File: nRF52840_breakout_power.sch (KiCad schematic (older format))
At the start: 18 parts, among them J7 Conn_01x02, Q1 DMG2395, SW1 SW_Push, U3 AP2112K-3.3, U4 MCP73831-2-OT

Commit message: changed crystal load capacitance according to component / minor changes
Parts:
- C29, C30, C31, C32: footprint (none) -> Capacitor_SMD:C_0805_2012Metric_Pad1.15x1.40mm_HandSolder
- D2: footprint (none) -> Diode_SMD:D_SOD-123F
- D3: footprint (none) -> LED_SMD:LED_0805_2012Metric_Pad1.15x1.40mm_HandSolder
- J7: value Conn_01x02 -> JST PH; footprint (none) -> Connector_JST:JST_PH_B2B-PH-SM4-TB_1x02-1MP_P2.00mm_Vertical
- Q1: footprint (none) -> Package_TO_SOT_SMD:SOT-23
- R10, R11, R5, R6, R7, R8, R9: footprint (none) -> Resistor_SMD:R_0805_2012Metric_Pad1.15x1.40mm_HandSolder
- SW1: footprint (none) -> Button_Switch_SMD:SW_SPST_EVQP7A
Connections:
- wire segments 56 -> 54
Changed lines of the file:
@@
 L Connector_Generic:Conn_01x02 J7
 U 1 1 5C935480
-P 1300 1700
-F 0 "J7" H 1220 1375 50  0000 C CNN
-F 1 "Conn_01x02" H 1220 1466 50  0000 C CNN
-F 2 "" H 1300 1700 50  0001 C CNN
-F 3 "~" H 1300 1700 50  0001 C CNN
-	1    1300 1700
+P 1350 1700
+F 0 "J7" H 1270 1375 50  0000 C CNN
+F 1 "JST PH" H 1270 1466 50  0000 C CNN
+F 2 "Connector_JST:JST_PH_B2B-PH-SM4-TB_1x02-1MP_P2.00mm_Vertical" H 1350 1700 50  0001 C CNN
+F 3 "~" H 1350 1700 50  0001 C CNN
+	1    1350 1700
 	-1   0    0    1
 $EndComp
@@
 F 0 "Q1" H 5555 1596 50  0000 L CNN
 F 1 "DMG2395" H 5555 1505 50  0000 L CNN
-F 2 "" H 5550 1475 50  0001 L CIN
+F 2 "Package_TO_SOT_SMD:SOT-23" H 5550 1475 50  0001 L CIN
 F 3 "http://www.vishay.com/docs/70209/70209.pdf" H 5350 1550 50  0001 L CNN
 	1    5350 1550
@@
 F 0 "D2" H 5200 1784 50  0000 C CNN
 F 1 "MBR120" H 5200 1875 50  0000 C CNN
-F 2 "" H 5200 2000 50  0001 C CNN
+F 2 "Diode_SMD:D_SOD-123F" H 5200 2000 50  0001 C CNN
 F 3 "~" H 5200 2000 50  0001 C CNN
 	1    5200 2000
@@
 F 0 "R8" H 4742 2304 50  0000 R CNN
 F 1 "100k" H 4742 2395 50  0000 R CNN
-F 2 "" H 4800 2350 50  0001 C CNN
+F 2 "Resistor_SMD:R_0805_2012Metric_Pad1.15x1.40mm_HandSolder" H 4800 2350 50  0001 C CNN
 F 3 "~" H 4800 2350 50  0001 C CNN
 	1    4800 2350
@@
 F 0 "C30" H 5542 2396 50  0000 L CNN
 F 1 "10µF" H 5542 2305 50  0000 L CNN
-F 2 "" H 5450 2350 50  0001 C CNN
+F 2 "Capacitor_SMD:C_0805_2012Metric_Pad1.15x1.40mm_HandSolder" H 5450 2350 50  0001 C CNN
 F 3 "~" H 5450 2350 50  0001 C CNN
 	1    5450 2350
@@
 F 0 "R9" H 5992 2304 50  0000 R CNN
 F 1 "100k" H 5992 2395 50  0000 R CNN
-F 2 "" H 6050 2350 50  0001 C CNN
+F 2 "Resistor_SMD:R_0805_2012Metric_Pad1.15x1.40mm_HandSolder" H 6050 2350 50  0001 C CNN
 F 3 "~" H 6050 2350 50  0001 C CNN
 	1    6050 2350
@@
 F 0 "C31" H 7242 2196 50  0000 L CNN
 F 1 "10µF" H 7242 2105 50  0000 L CNN
-F 2 "" H 7150 2150 50  0001 C CNN
+F 2 "Capacitor_SMD:C_0805_2012Metric_Pad1.15x1.40mm_HandSolder" H 7150 2150 50  0001 C CNN
 F 3 "~" H 7150 2150 50  0001 C CNN
 	1    7150 2150
@@
 F 0 "R11" H 10459 1496 50  0000 L CNN
 F 1 "5k" H 10459 1405 50  0000 L CNN
-F 2 "" H 10400 1450 50  0001 C CNN
+F 2 "Resistor_SMD:R_0805_2012Metric_Pad1.15x1.40mm_HandSolder" H 10400 1450 50  0001 C CNN
 F 3 "~" H 10400 1450 50  0001 C CNN
 	1    10400 1450
@@
 F 0 "C32" H 9392 1996 50  0000 L CNN
 F 1 "10µF" H 9392 1905 50  0000 L CNN
-F 2 "" H 9300 1950 50  0001 C CNN
+F 2 "Capacitor_SMD:C_0805_2012Metric_Pad1.15x1.40mm_HandSolder" H 9300 1950 50  0001 C CNN
 F 3 "~" H 9300 1950 50  0001 C CNN
 	1    9300 1950
@@
 F 0 "D3" H 8792 1295 50  0000 C CNN
 F 1 "LED" H 8792 1386 50  0000 C CNN
-F 2 "" H 8800 1550 50  0001 C CNN
+F 2 "LED_SMD:LED_0805_2012Metric_Pad1.15x1.40mm_HandSolder" H 8800 1550 50  0001 C CNN
 F 3 "~" H 8800 1550 50  0001 C CNN
 	1    8800 1550
@@
 F 0 "R10" V 9004 1550 50  0000 C CNN
 F 1 "100k" V 9095 1550 50  0000 C CNN
-F 2 "" H 9200 1550 50  0001 C CNN
+F 2 "Resistor_SMD:R_0805_2012Metric_Pad1.15x1.40mm_HandSolder" H 9200 1550 50  0001 C CNN
 F 3 "~" H 9200 1550 50  0001 C CNN
 	1    9200 1550
@@
 F 0 "R7" H 3242 1804 50  0000 R CNN
 F 1 "100k" H 3242 1895 50  0000 R CNN
-F 2 "" H 3300 1850 50  0001 C CNN
+F 2 "Resistor_SMD:R_0805_2012Metric_Pad1.15x1.40mm_HandSolder" H 3300 1850 50  0001 C CNN
 F 3 "~" H 3300 1850 50  0001 C CNN
 	1    3300 1850
@@
 F 0 "R6" H 3242 1404 50  0000 R CNN
 F 1 "100k" H 3242 1495 50  0000 R CNN
-F 2 "" H 3300 1450 50  0001 C CNN
+F 2 "Resistor_SMD:R_0805_2012Metric_Pad1.15x1.40mm_HandSolder" H 3300 1450 50  0001 C CNN
 F 3 "~" H 3300 1450 50  0001 C CNN
 	1    3300 1450
@@
 Wire Wire Line
 	3300 1950 3300 2000
-Wire Wire Line
-	1500 1600 1550 1600
-Wire Wire Line
-	1500 1700 1550 1700
 Wire Wire Line
 	1550 1700 1550 1750
@@
 F 0 "SW1" H 1150 3885 50  0000 C CNN
 F 1 "SW_Push" H 1150 3794 50  0000 C CNN
-F 2 "" H 1150 3800 50  0001 C CNN
+F 2 "Button_Switch_SMD:SW_SPST_EVQP7A" H 1150 3800 50  0001 C CNN
 F 3 "~" H 1150 3800 50  0001 C CNN
 	1    1150 3600
@@
 F 0 "R5" H 1559 3446 50  0000 L CNN
 F 1 "10k" H 1559 3355 50  0000 L CNN
-F 2 "" H 1500 3400 50  0001 C CNN
+F 2 "Resistor_SMD:R_0805_2012Metric_Pad1.15x1.40mm_HandSolder" H 1500 3400 50  0001 C CNN
 F 3 "~" H 1500 3400 50  0001 C CNN
 	1    1500 3400
@@
 F 0 "C29" H 1592 3846 50  0000 L CNN
 F 1 "100nF" H 1592 3755 50  0000 L CNN
-F 2 "" H 1500 3800 50  0001 C CNN
+F 2 "Capacitor_SMD:C_0805_2012Metric_Pad1.15x1.40mm_HandSolder" H 1500 3800 50  0001 C CNN
 F 3 "~" H 1500 3800 50  0001 C CNN
 	1    1500 3800

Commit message: minor changes to schematic and layout
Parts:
- removed J7: JST PH, Connector_JST:JST_PH_B2B-PH-SM4-TB_1x02-1MP_P2.00mm_Vertical, symbol Connector_Generic:Conn_01x02
- added J7: S2B-PH-SM4-TB(LF)(SN), custom_footprints:JST_PH_S2B-PH-SM4-TB_LF__SN_, symbol JST_PH_S2B-PH-SM4-TB_LF__SN_:S2B-PH-SM4-TB(LF)(SN)
- SW1: footprint Button_Switch_SMD:SW_SPST_EVQP7A -> Button_Switch_SMD:SW_SPST_TL3342
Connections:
- wire segments 54 -> 58
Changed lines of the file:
@@
 $Descr A4 11693 8268
 encoding utf-8
-Sheet 3 3
+Sheet 3 4
 Title "nRF52840_breakout"
 Date "2019-03-22"
@@
 Comment4 ""
 $EndDescr
-$Comp
-L Connector_Generic:Conn_01x02 J7
-U 1 1 5C935480
-P 1350 1700
-F 0 "J7" H 1270 1375 50  0000 C CNN
-F 1 "JST PH" H 1270 1466 50  0000 C CNN
-F 2 "Connector_JST:JST_PH_B2B-PH-SM4-TB_1x02-1MP_P2.00mm_Vertical" H 1350 1700 50  0001 C CNN
-F 3 "~" H 1350 1700 50  0001 C CNN
-	1    1350 1700
-	-1   0    0    1
-$EndComp
 Text Notes 600  650  0    50   ~ 0
 LiPo Connector
@@
 VDD_BAT
 $Comp
-L power:GND #PWR034
+L power:GND #PWR035
 U 1 1 5C93551C
-P 1550 1750
-F 0 "#PWR034" H 1550 1500 50  0001 C CNN
-F 1 "GND" H 1555 1577 50  0000 C CNN
-F 2 "" H 1550 1750 50  0001 C CNN
-F 3 "" H 1550 1750 50  0001 C CNN
-	1    1550 1750
+P 1550 2000
+F 0 "#PWR035" H 1550 1750 50  0001 C CNN
+F 1 "GND" H 1555 1827 50  0000 C CNN
+F 2 "" H 1550 2000 50  0001 C CNN
+F 3 "" H 1550 2000 50  0001 C CNN
+	1    1550 2000
 	1    0    0    -1
 $EndComp
@@
 	4800 2000 4800 2250
 $Comp
-L power:GND #PWR036
+L power:GND #PWR037
 U 1 1 5C936C7B
 P 4800 2500
-F 0 "#PWR036" H 4800 2250 50  0001 C CNN
+F 0 "#PWR037" H 4800 2250 50  0001 C CNN
 F 1 "GND" H 4805 2327 50  0000 C CNN
 F 2 "" H 4800 2500 50  0001 C CNN
@@
 $EndComp
 $Comp
-L power:GND #PWR037
+L power:GND #PWR038
 U 1 1 5C936C9F
 P 5450 2500
-F 0 "#PWR037" H 5450 2250 50  0001 C CNN
+F 0 "#PWR038" H 5450 2250 50  0001 C CNN
 F 1 "GND" H 5455 2327 50  0000 C CNN
 F 2 "" H 5450 2500 50  0001 C CNN
@@
 	7150 2250 7150 2300
 $Comp
-L power:GND #PWR039
+L power:GND #PWR040
 U 1 1 5C9377BD
 P 7150 2300
-F 0 "#PWR039" H 7150 2050 50  0001 C CNN
+F 0 "#PWR040" H 7150 2050 50  0001 C CNN
 F 1 "GND" H 7155 2127 50  0000 C CNN
 F 2 "" H 7150 2300 50  0001 C CNN
@@
 	10400 1250 10400 1100
 $Comp
-L power:GND #PWR041
+L power:GND #PWR042
 U 1 1 5C937FE3
 P 10400 1100
-F 0 "#PWR041" H 10400 850 50  0001 C CNN
+F 0 "#PWR042" H 10400 850 50  0001 C CNN
 F 1 "GND" H 10405 927 50  0000 C CNN
 F 2 "" H 10400 1100 50  0001 C CNN
@@
 $EndComp
 $Comp
-L power:GND #PWR040
+L power:GND #PWR041
 U 1 1 5C93810D
 P 9300 2100
-F 0 "#PWR040" H 9300 1850 50  0001 C CNN
+F 0 "#PWR041" H 9300 1850 50  0001 C CNN
 F 1 "GND" H 9305 1927 50  0000 C CNN
 F 2 "" H 9300 2100 50  0001 C CNN
@@
 VDIV
 $Comp
-L power:GND #PWR035
+L power:GND #PWR036
 U 1 1 5C93BC33
 P 3300 2000
-F 0 "#PWR035" H 3300 1750 50  0001 C CNN
+F 0 "#PWR036" H 3300 1750 50  0001 C CNN
 F 1 "GND" H 3305 1827 50  0000 C CNN
 F 2 "" H 3300 2000 50  0001 C CNN
@@
 Wire Wire Line
 	3300 1950 3300 2000
-Wire Wire Line
-	1550 1700 1550 1750
-$Comp
-L power:GND #PWR038
+$Comp
+L power:GND #PWR039
 U 1 1 5C93E165
 P 6750 2450
-F 0 "#PWR038" H 6750 2200 50  0001 C CNN
+F 0 "#PWR039" H 6750 2200 50  0001 C CNN
 F 1 "GND" H 6755 2277 50  0000 C CNN
 F 2 "" H 6750 2450 50  0001 C CNN
@@
 F 0 "SW1" H 1150 3885 50  0000 C CNN
 F 1 "SW_Push" H 1150 3794 50  0000 C CNN
-F 2 "Button_Switch_SMD:SW_SPST_EVQP7A" H 1150 3800 50  0001 C CNN
+F 2 "Button_Switch_SMD:SW_SPST_TL3342" H 1150 3800 50  0001 C CNN
 F 3 "~" H 1150 3800 50  0001 C CNN
 	1    1150 3600
@@
 $EndComp
 $Comp
-L power:GND #PWR032
+L power:GND #PWR033
 U 1 1 5C95A0F8
 P 900 3600
-F 0 "#PWR032" H 900 3350 50  0001 C CNN
+F 0 "#PWR033" H 900 3350 50  0001 C CNN
 F 1 "GND" V 905 3472 50  0000 R CNN
 F 2 "" H 900 3600 50  0001 C CNN
@@
 VDD_nRF
 $Comp
-L power:GND #PWR033
+L power:GND #PWR034
 U 1 1 5C95B811
 P 1500 3950
-F 0 "#PWR033" H 1500 3700 50  0001 C CNN
+F 0 "#PWR034" H 1500 3700 50  0001 C CNN
 F 1 "GND" H 1505 3777 50  0000 C CNN
 F 2 "" H 1500 3950 50  0001 C CNN
@@
 	-1   0    0    1
 $EndComp
+$Comp
+L JST_PH_S2B-PH-SM4-TB_LF__SN_:S2B-PH-SM4-TB(LF)(SN) J7
+U 1 1 5C9B04BC
+P 1200 1700
+F 0 "J7" H 1119 2065 50  0000 C CNN
+F 1 "S2B-PH-SM4-TB(LF)(SN)" H 1119 1974 50  0000 C CNN
+F 2 "custom_footprints:JST_PH_S2B-PH-SM4-TB_LF__SN_" H 1200 1700 50  0001 L BNN
+F 3 "S2B-PH-SM4-TB_LF__SN_" H 1200 1700 50  0001 L BNN
+F 4 "https://www.digikey.de/product-detail/en/jst-sales-america-inc/S2B-PH-SM4-TB_LF__SN_/455-1749-1-ND/926846?utm_source=snapeda&utm_medium=aggregator&utm_campaign=symbol" H 1200 1700 50  0001 L BNN "Field4"
+F 5 "455-1749-1-ND" H 1200 1700 50  0001 L BNN "Field5"
+F 6 "None" H 1200 1700 50  0001 L BNN "Field6"
+F 7 "JST Sales" H 1200 1700 50  0001 L BNN "Field7"
+F 8 "PH Series 2 Position 2 mm Pitch Surface Mount Side Entry Shrouded Header" H 1200 1700 50  0001 L BNN "Field8"
+	1    1200 1700
+	-1   0    0    -1
+$EndComp
+Wire Wire Line
+	1500 1700 1550 1700
+Wire Wire Line
+	1550 1700 1550 1900
+Wire Wire Line
+	1500 1900 1550 1900
+Connection ~ 1550 1900
+Wire Wire Line
+	1550 1900 1550 2000
+Wire Wire Line
+	1500 1600 1550 1600
 $EndSCHEMATC

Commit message: added som like version of the breakout
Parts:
- removed C29: 100nF, Capacitor_SMD:C_0805_2012Metric_Pad1.15x1.40mm_HandSolder, symbol Device:C_Small
- removed C32: 10µF, Capacitor_SMD:C_0805_2012Metric_Pad1.15x1.40mm_HandSolder, symbol Device:C_Small
- removed D3: LED, LED_SMD:LED_0805_2012Metric_Pad1.15x1.40mm_HandSolder, symbol Device:LED
- removed J7: S2B-PH-SM4-TB(LF)(SN), custom_footprints:JST_PH_S2B-PH-SM4-TB_LF__SN_, symbol JST_PH_S2B-PH-SM4-TB_LF__SN_:S2B-PH-SM4-TB(LF)(SN)
- removed R10, R6, R7: 100k, Resistor_SMD:R_0805_2012Metric_Pad1.15x1.40mm_HandSolder, symbol Device:R_Small
- removed R11: 5k, Resistor_SMD:R_0805_2012Metric_Pad1.15x1.40mm_HandSolder, symbol Device:R_Small
- removed R5: 10k, Resistor_SMD:R_0805_2012Metric_Pad1.15x1.40mm_HandSolder, symbol Device:R_Small
- removed SW1: SW_Push, Button_Switch_SMD:SW_SPST_TL3342, symbol Switch:SW_Push
- removed U4: MCP73831-2-OT, Package_TO_SOT_SMD:SOT-23-5, symbol mcp73832-2-ot:MCP73831-2-OT
- added D2: LED_RED, LED_SMD:LED_0402_1005Metric, symbol Device:LED_Small
- added R3: 1k, Resistor_SMD:R_0402_1005Metric, symbol Device:R_Small
- C23: renamed from C30; footprint Capacitor_SMD:C_0805_2012Metric_Pad1.15x1.40mm_HandSolder -> Capacitor_SMD:C_0402_1005Metric
- C24: renamed from C31; footprint Capacitor_SMD:C_0805_2012Metric_Pad1.15x1.40mm_HandSolder -> Capacitor_SMD:C_0402_1005Metric
- R1: renamed from R8; footprint Resistor_SMD:R_0805_2012Metric_Pad1.15x1.40mm_HandSolder -> Resistor_SMD:R_0402_1005Metric
- R2: renamed from R9; footprint Resistor_SMD:R_0805_2012Metric_Pad1.15x1.40mm_HandSolder -> Resistor_SMD:R_0402_1005Metric
- renumbered D2 to D1, U3 to U2
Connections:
- net labels removed: P1.18_RESET, VDIV
- wire segments 58 -> 28
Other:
- note removed: "10k = 100mA\n5k = 200mA\n2k = 500mA\n1k = 1A"
- note removed: "Battery Status"
- note removed: "Charging Circuit"
- note removed: "LiPo Connector"
- note removed: "Reset Switch\n"
- moved on the sheet: C23, C24, R1, R2, U2

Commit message: path selection/charging/bme680 sensor integration
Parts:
- removed D1: MBR120, Diode_SMD:D_SOD-123F, symbol Device:D_Schottky
- removed Q1: DMG2395, Package_TO_SOT_SMD:SOT-23, symbol Transistor_FET:BS250
- removed U2: AP2112K-3.3, Package_TO_SOT_SMD:SOT-23-5, symbol Regulator_Linear:AP2112K-3.3
- added C1, C2, C27: 10µF, Capacitor_SMD:C_0402_1005Metric, symbol Device:C_Small
- added C26: 0.1µF, Capacitor_SMD:C_0402_1005Metric, symbol Device:C_Small
- added D1: GRN, LED_SMD:LED_0402_1005Metric, symbol Device:LED_Small
- added J6: S2B-PH-SM4-TB(LF)(SN), custom_footprints:JST_PH_S2B-PH-SM4-TB_LF__SN_, symbol JST_PH_S2B-PH-SM4-TB_LF__SN_:S2B-PH-SM4-TB(LF)(SN)
- added L5: L_Small, Inductor_SMD:L_0402_1005Metric, symbol Device:L_Small
- added R6: 10k, Resistor_SMD:R_0402_1005Metric, symbol Device:R_Small
- added R7, R8: 1.5k, Resistor_SMD:R_0402_1005Metric, symbol Device:R_Small
- added U2: BQ24072, Package_DFN_QFN:VQFN-16-1EP_3x3mm_P0.5mm_EP1.68x1.68mm_ThermalVias, symbol BQ24072:BQ24072
- added U3: TPS63031, Package_SON:Texas_DRC0010J_ThermalVias, symbol tps63031:TPS63031
- D2: value LED_RED -> RED
- R1: value 100k -> 46.4k
- R2: value 100k -> 1.18k
- R3: value 1k -> 1.13k
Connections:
- net labels added: P0.26, P0.27, V_SYS
- wire segments 28 -> 73
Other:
- note removed: "Power Selection 600mA Output"

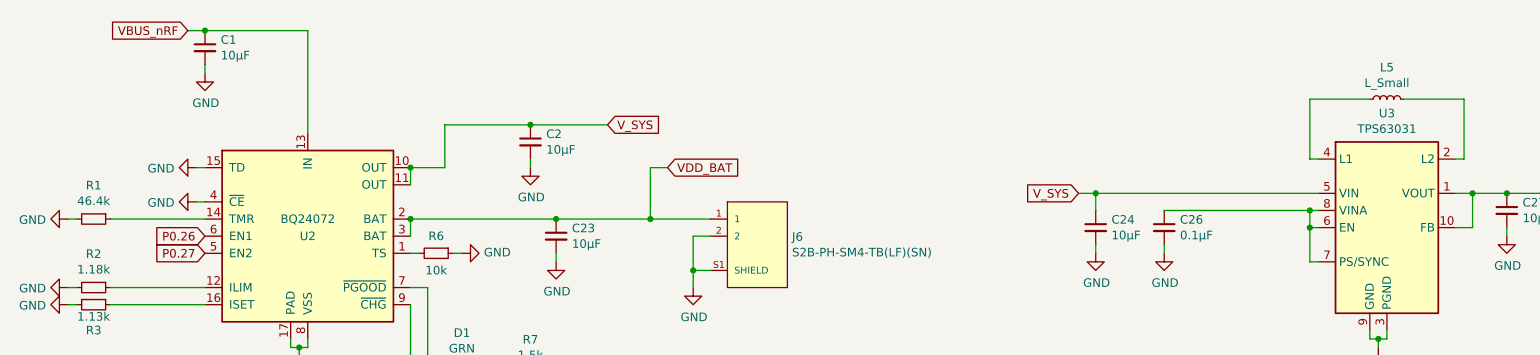
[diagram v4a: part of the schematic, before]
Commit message: minor changes / switched from tag - 10pol debug connector
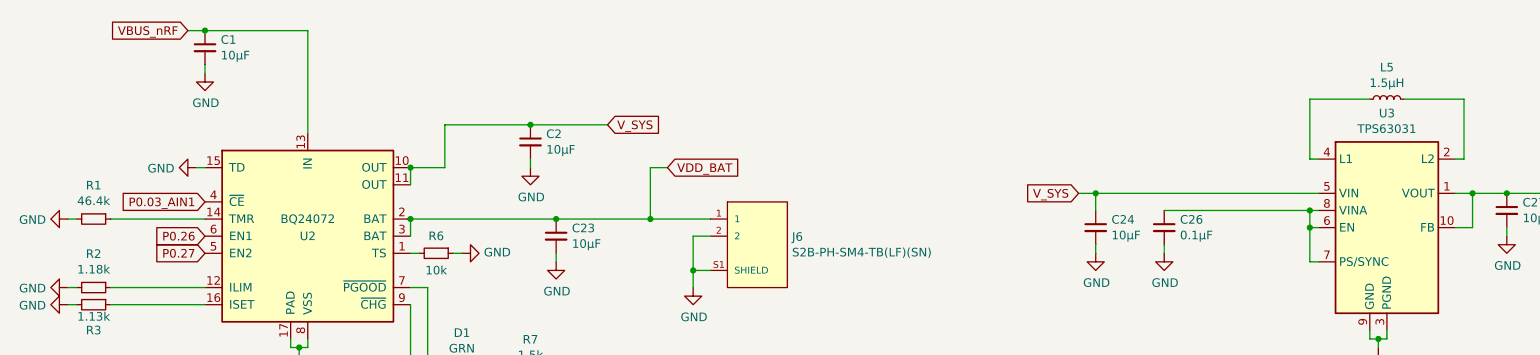
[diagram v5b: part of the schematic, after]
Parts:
- L5: value L_Small -> 1.5µH
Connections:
- net GND: no longer U2.4 (~CE)
- new net P0.03_AIN1: U2.4 (~CE)
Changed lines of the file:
@@
-$EndComp
-$Comp
-L power:GND #PWR0110
-U 1 1 5CC24F90
-P 1650 1650
-F 0 "#PWR0110" H 1650 1400 50  0001 C CNN
-F 1 "GND" V 1655 1522 50  0000 R CNN
-F 2 "" H 1650 1650 50  0001 C CNN
-F 3 "" H 1650 1650 50  0001 C CNN
-	1    1650 1650
-	0    1    1    0
 $EndComp
 $Comp
@@
 Wire Wire Line
 	1650 1450 1700 1450
-Wire Wire Line
-	1650 1650 1700 1650
 Wire Wire Line
 	900  1750 950  1750
@@
 P 8600 1050
 F 0 "L5" V 8785 1050 50  0000 C CNN
-F 1 "L_Small" V 8694 1050 50  0000 C CNN
+F 1 "1.5µH" V 8694 1050 50  0000 C CNN
 F 2 "Inductor_SMD:L_0402_1005Metric" H 8600 1050 50  0001 C CNN
 F 3 "~" H 8600 1050 50  0001 C CNN
@@
 Wire Wire Line
 	4300 1750 4650 1750
+Text GLabel 1700 1650 0    50   Input ~ 0
+P0.03_AIN1
 $EndSCHEMATC

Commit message: layout / added part details etc
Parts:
- C24, C27: Part (none) -> GRM188R60J106KME84D,Murata
- C26: Part (none) -> 0.1μF, X7Rceramic
- L5: Part (none) -> LPS3015-1R5,Coilcraft
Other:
- note added: "Buck-Boost Converter\n800mA Output"
- note added: "Note:\n-Pin 3 and 11 changed to passive for ERC"
- note added: "Power path management and charging"
- moved on the sheet: C1, C2, C23, C24, C26, C27, D1, D2, J6, L5, R1, R2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
